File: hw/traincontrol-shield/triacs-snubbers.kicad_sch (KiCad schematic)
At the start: 6 parts, among them Q1 BT134W-600D, Q2 BT134W-600D

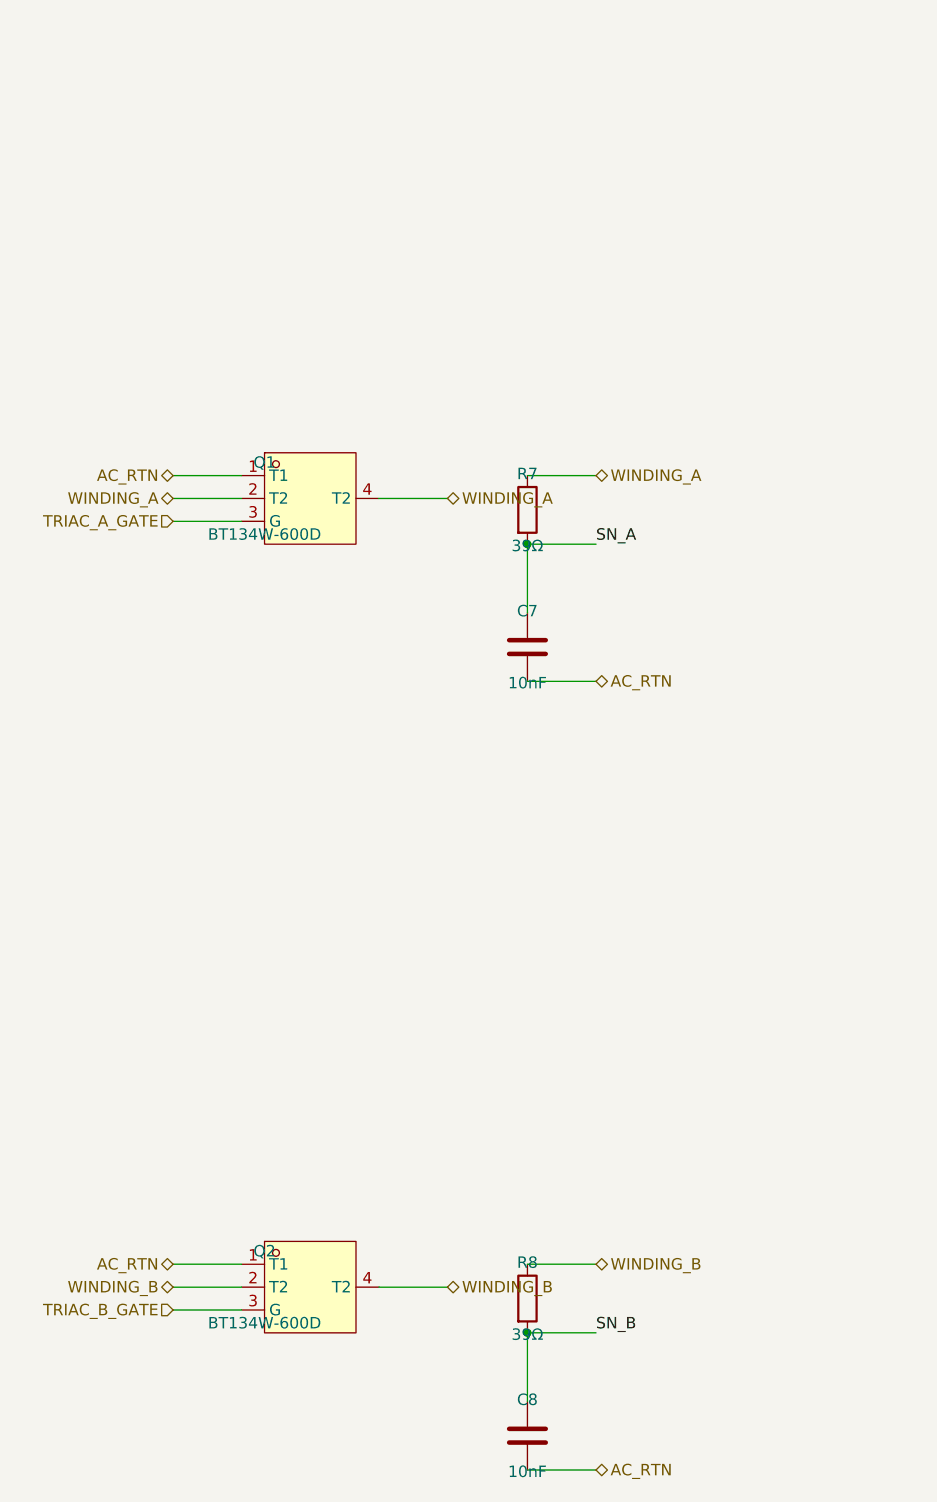
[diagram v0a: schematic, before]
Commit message: Schematic updates by hand.
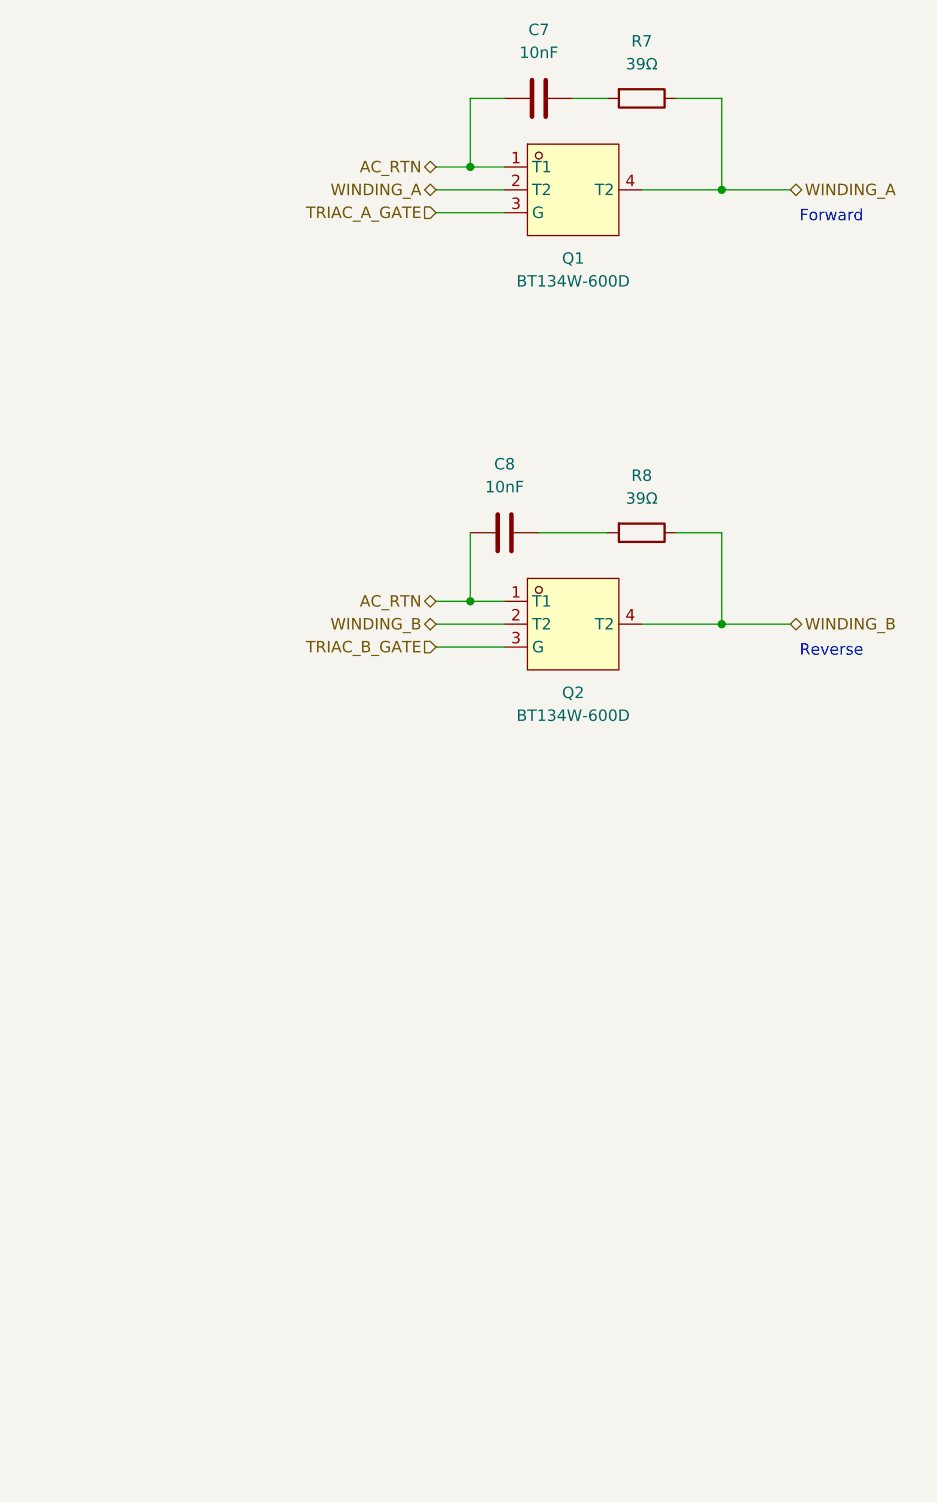
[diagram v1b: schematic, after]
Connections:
- net SN_A: no longer names the net of C7.1, R7.2
- net SN_B: no longer names the net of C8.1, R8.2
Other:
- note added: "Forward"
- note added: "Reverse"
- moved on the sheet: C7, C8, Q1, Q2, R7, R8
